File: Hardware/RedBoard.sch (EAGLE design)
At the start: 65 parts, among them IC3 LM1117, J2 ICSP, J3 POWER_JACKSUPER_BOMB_DIGITY, Q1 1A/60V/500mΩ, Q2 2N7002PW, U1 FT231XS, U2 MIC5205, U4 ATMEGA328P_TQFP, Y1 16MHz

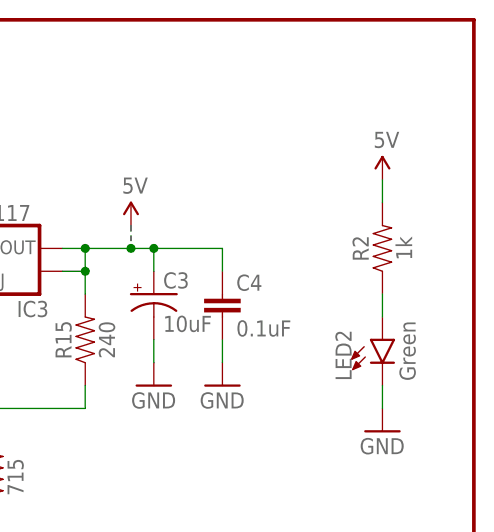
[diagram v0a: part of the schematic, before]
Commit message: Fixing LED silk, changing power LED resistor.
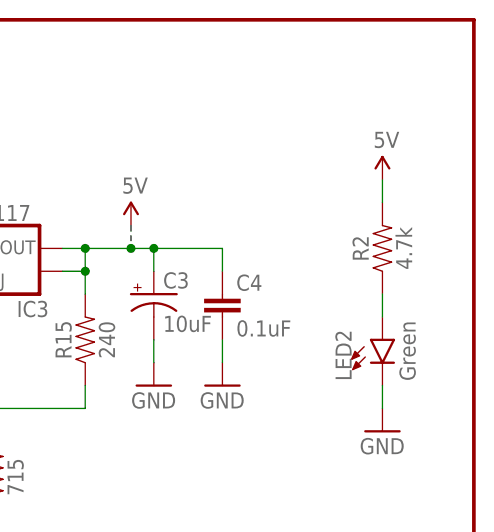
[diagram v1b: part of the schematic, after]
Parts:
- R2: value 1k -> 4.7k; device SparkFun-Resistors:1KOHM-0603-1/10W-1% -> SparkFun-Resistors:4.7KOHM-0603-1/10W-1%
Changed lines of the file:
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@@
 <part name="R1" library="SparkFun-Resistors" deviceset="1KOHM" device="-0603-1/10W-1%" value="1k"/>
 <part name="GND3" library="SparkFun" deviceset="GND" device=""/>
-<part name="R2" library="SparkFun-Resistors" deviceset="1KOHM" device="-0603-1/10W-1%" value="1k"/>
+<part name="R2" library="SparkFun-Resistors" deviceset="4.7KOHM" device="-0603-1/10W-1%" value="4.7k"/>
 <part name="U$2" library="SparkFun" deviceset="5V" device=""/>
 <part name="GND4" library="SparkFun" deviceset="GND" device=""/>

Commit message: Fixing PROD_ID on J2 and C10.
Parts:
- C10: device SparkFun-Capacitors:0.1UF-0603-25V-5% -> SparkFun-Capacitors:0.1UF-0603-25V-(+80/-20%)
- J2: PROD_ID (none) -> CONN-11415
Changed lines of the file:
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@@
 <?xml version="1.0" encoding="utf-8"?>
 <!DOCTYPE eagle SYSTEM "eagle.dtd">
-<eagle version="7.5.0">
+<eagle version="7.6.0">
 <drawing>
 <settings>
@@
 <part name="U$8" library="SparkFun" deviceset="5V" device=""/>
 <part name="C8" library="SparkFun-Capacitors" deviceset="0.1UF" device="-0603-25V-(+80/-20%)" value="0.1uF"/>
-<part name="C10" library="SparkFun-Capacitors" deviceset="0.1UF" device="-0603-25V-5%" value="0.1uF"/>
+<part name="C10" library="SparkFun-Capacitors" deviceset="0.1UF" device="-0603-25V-(+80/-20%)" value="0.1uF"/>
 <part name="GND24" library="SparkFun" deviceset="GND" device=""/>
 <part name="IC3" library="Testing" deviceset="V_REG_LM1117" device="ALT1" value="LM1117">
@@
 <part name="JP1" library="SparkFun-Aesthetics" deviceset="SFE_LOGO_NAME" device=".1_INCH"/>
 <part name="JP7" library="SparkFun-Aesthetics" deviceset="SFE_LOGO_FLAME" device=".1_INCH"/>
-<part name="J2" library="SparkFun-Connectors" deviceset="AVR_SPI_PROG_3X2" device="SMD" value="ICSP"/>
+<part name="J2" library="SparkFun-Connectors" deviceset="AVR_SPI_PROG_3X2" device="SMD" value="ICSP">
+<attribute name="PROD_ID" value="CONN-11415"/>
+</part>
 <part name="C6" library="SparkFun-Capacitors" deviceset="10UF-POLAR" device="-EIA3216-16V-10%(TANT)" value="10uF"/>
 <part name="GND14" library="SparkFun" deviceset="GND" device=""/>

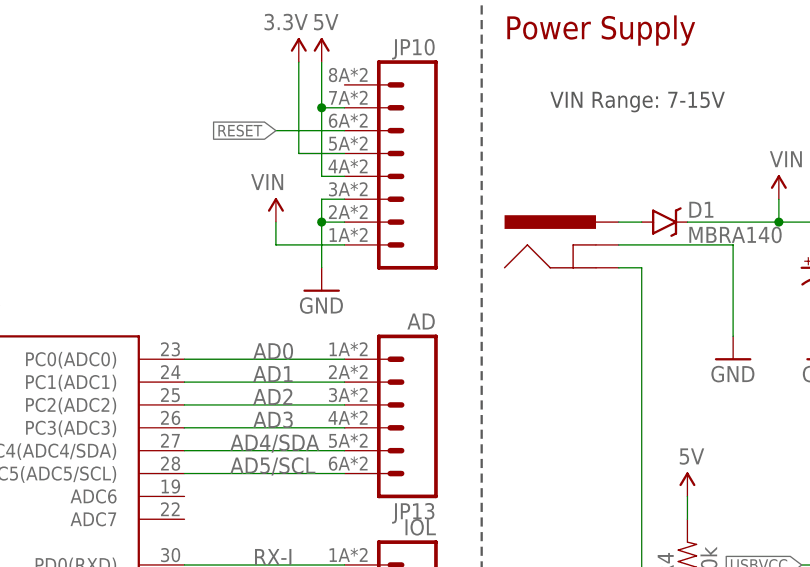
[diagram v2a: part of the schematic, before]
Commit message: Component Values Updated for 3D Model
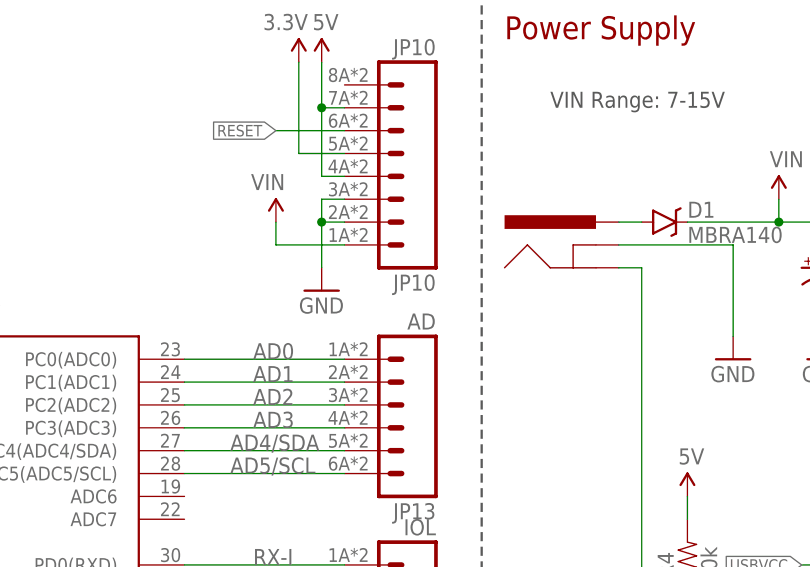
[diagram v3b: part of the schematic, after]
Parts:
- JP10: value (none) -> JP10
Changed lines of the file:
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@@
 <?xml version="1.0" encoding="utf-8"?>
 <!DOCTYPE eagle SYSTEM "eagle.dtd">
-<eagle version="7.6.0">
+<eagle version="7.7.0">
 <drawing>
 <settings>
@@
 <attribute name="PROD_ID" value="CONN-11219"/>
 </part>
-<part name="JP10" library="SparkFun-Connectors" deviceset="M08" device="SMD-COMBO">
+<part name="JP10" library="SparkFun-Connectors" deviceset="M08" device="SMD-COMBO" value="JP10">
 <attribute name="PROD_ID" value="CONN-10204"/>
 </part>

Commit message: Starting from BlackBoard x02
Starting from BlackBoard x02
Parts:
- removed C13, C9: 47pF, SparkFun-Capacitors:47PF-0603-50V-5%
- removed C14: 0.1uF, SparkFun-Capacitors:0.1UF-0603-25V-(+80/-20%)
- removed JP12: USB-MINIB-5PIN, SparkFun-Connectors:USB-MINIB-5PIN
- removed LED3: Red, SparkFun-LED:LED1206
- removed LED4: Yellow, SparkFun-LED:LED1206
- removed R10: 27, SparkFun-Resistors:27OHM-0603-1/10W-1%
- removed R7, R8, R9: 1k, SparkFun-Resistors:1KOHM-0603-1/10W-1%
- removed U1: FT231XS, SparkFun-IC-Comms:FT231XS
- added C11: 22pF, SparkFun-Capacitors:22PF-0603-50V-5%
- added C16: 1.0uF, SparkFun-Capacitors:1.0UF-16V-10%(0603)
- added C17: 10nF, SparkFun-Capacitors:10NF/10000PF-50V-10%(0603)
- added C18: 0.1uF, SparkFun-Capacitors:0.1UF-25V(+80/-20%)(0603)
- added D3: Yellow, SparkFun-LED:LED-YELLOW_HIDDENSILK
- added I/O: JUMPER-SMT_3_1-NC_TRACE_SILK, SparkFun-Jumpers:JUMPER-SMT_3_1-NC_TRACE_SILK
- added J1: AMP FCI 10103594-0001LF, SparkFun-Connectors:USB_MICRO-B_HALF_PTH_MILL
- added J4: (no value), SparkFun-Connectors:QWIIC_CONNECTORJS-1MM
- added LED5: GREEN, SparkFun-LED:LED-GREEN_HIDDENSILK
- added Q3: 2N7002PW, SparkFun-DiscreteSemi:MOSFET-NCH-2N7002PW
- added R12, R16: 4.7k, SparkFun-Resistors:4.7KOHM-0603-1/10W-1%
- added U3: AP2112-3.3V, SparkFun-PowerIC:V_REG_AP2112K-3.3V
- added Y2: 12MHz, USB Basic:CRYSTAL-GROUNDED3.2X2.5
- C7: value 1.0uF -> 22pF; device SparkFun-Capacitors:1.0UF-0603-16V-10% -> SparkFun-Capacitors:22PF-0603-50V-5%
- D1: value MBRA140 -> SS14TR
- F1: value 6V/0.5A -> PPTC_6V500MA; device SparkFun-Fuses:PTC-HALF_AMP -> SparkFun-Fuses:PPTC_6V500MA
- J2: value ICSP -> ISP
- JP10: value JP10 -> (none)
- JP11: value IOL -> JP11
- JP13: value AD -> (none)
- LED1: device SparkFun-LED:LED1206 -> SparkFun-LED:LED-BLUE_HIDDENSILK
- LED2: value Green -> GREEN; device SparkFun-LED:LED1206 -> SparkFun-LED:LED-GREEN_HIDDENSILK
- R1: value 1k -> 4.7k; device SparkFun-Resistors:1KOHM-0603-1/10W-1% -> SparkFun-Resistors:4.7KOHM-0603-1/10W-1%
- R11, R13: value 10k -> 2.2k; device SparkFun-Resistors:10KOHM-0603-1/10W-1% -> SparkFun-Resistors:2.2KOHM-0603-1/10W-1%
- R2: value 4.7k -> 10k; device SparkFun-Resistors:4.7KOHM-0603-1/10W-1% -> SparkFun-Resistors:10KOHM-0603-1/10W-1%
- R5: value 27 -> 2.2k; device SparkFun-Resistors:27OHM-0603-1/10W-1% -> SparkFun-Resistors:2.2KOHM-0603-1/10W-1%
- R6: value 1k -> 2.2k; device SparkFun-Resistors:1KOHM-0603-1/10W-1% -> SparkFun-Resistors:2.2KOHM-0603-1/10W-1%
- U2: value MIC5205 -> CH340G; device SparkFun-PowerIC:MIC52053.3V -> SparkFun-DigitalIC:CH340GSMD
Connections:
- removed net 3.3V_F: C14.1, Q2.G, R11.2, U1.!RESET, U1.3V3OUT, U1.VCCIO
- removed net D+: C9.1, JP12.D+, R10.1
- removed net D-: C13.1, JP12.D-, R5.1
- removed net DTR: C8.1, Q2.D, R13.1
- removed net FTDI_DTR: Q2.S, R11.1, U1.!DTR
- removed net N$10: LED4.A, R7.2
- removed net N$6: R5.2, U1.USBDM
- removed net N$7: R10.2, U1.USBDP
- removed net N$8: LED3.A, R6.2
- removed net RXD: R9.2, U1.RXD
- removed net RXLED: LED4.C, U1.CBUS1
- removed net TXD: R8.2, U1.TXD
- removed net TXLED: LED3.C, U1.CBUS2
- new net !DTR: C8.1, U2.!DTR
- new net LV_SCL: J4.4, Q2.S, R11.1
- new net LV_SDA: J4.3, Q3.S, R5.1
- new net N$11: C11.2, U2.XO, Y2.2
- new net N$12: C7.2, U2.XI, Y2.1
- new net N$13: J1.D-, U2.UD-
- new net N$14: J1.D+, U2.UD+
- new net N$5: LED5.A, R16.1
- new net N$9: D3.A, R12.1
- new net SHLD: J1.SHIELD
- new net V3: C17.1, U2.V3
- new net VCC: C18.1, C2.2, I/O.2, J2.2, R12.2, R13.2, R16.2, R2.2, R3.2, R6.2, TP1.1, U2.VCC, U4.AVCC, U4.VCC@4, U4.VCC@6
- net 3.3V: now also C16.1, I/O.1, J4.2, Q2.G, Q3.G, R11.2, R5.2, U3.OUT; no longer C7.1, U2.OUT
- net 5V: now also I/O.3, U3.EN, U3.IN; no longer C2.2, J2.2, R13.2, R2.2, R3.2, R6.1, R7.1, TP1.1, U2.EN, U2.IN, U4.AVCC, U4.VCC@4, U4.VCC@6
- net AD4/SDA: now also Q3.D, R6.1
- net AD5/SCL: now also Q2.D, R13.1
- net GND: now also C11.1, C16.2, C17.2, C18.2, C7.1, J1.GND, J4.1, U3.GND, Y2.GND; no longer C13.2, C14.2, C7.2, C9.2, JP12.GND, JP12.MTN1, JP12.MTN2, JP12.MTN3, JP12.MTN4, U1.GND@16, U1.GND@6
- net RX-I: now also D3.C, U2.TXD; no longer R8.1
- net TX-O: now also LED5.C, U2.RXD; no longer R9.1
- net USBVCC: no longer U1.VCC
- net VUSB: now also J1.VBUS; no longer JP12.VBUS
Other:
- note added: "3.3V 600mA Out"
- note added: "Board I/O Voltage"
- note added: "Jim Lindblom, N. Seidle"
- note added: "Qwiic"
- note added: "Qwiic 3.3V Conversion"
- note added: "To convert the board to 3.3V you must cut the jumper to 5V and use solder to close the jumper towards 3.3V."
- note added: "USB-to-Serial Converter"
- note added: "X01"
- note removed: "3.3V 150mA Out"
- note removed: "FT231XS (USB-to-Serial Converter)"
- note removed: "Jim Lindblom"
- note removed: "v22"
- moved on the sheet: C10, C12, C15, C2, C3, C4, C5, C6, C7, C8, D1, IC3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

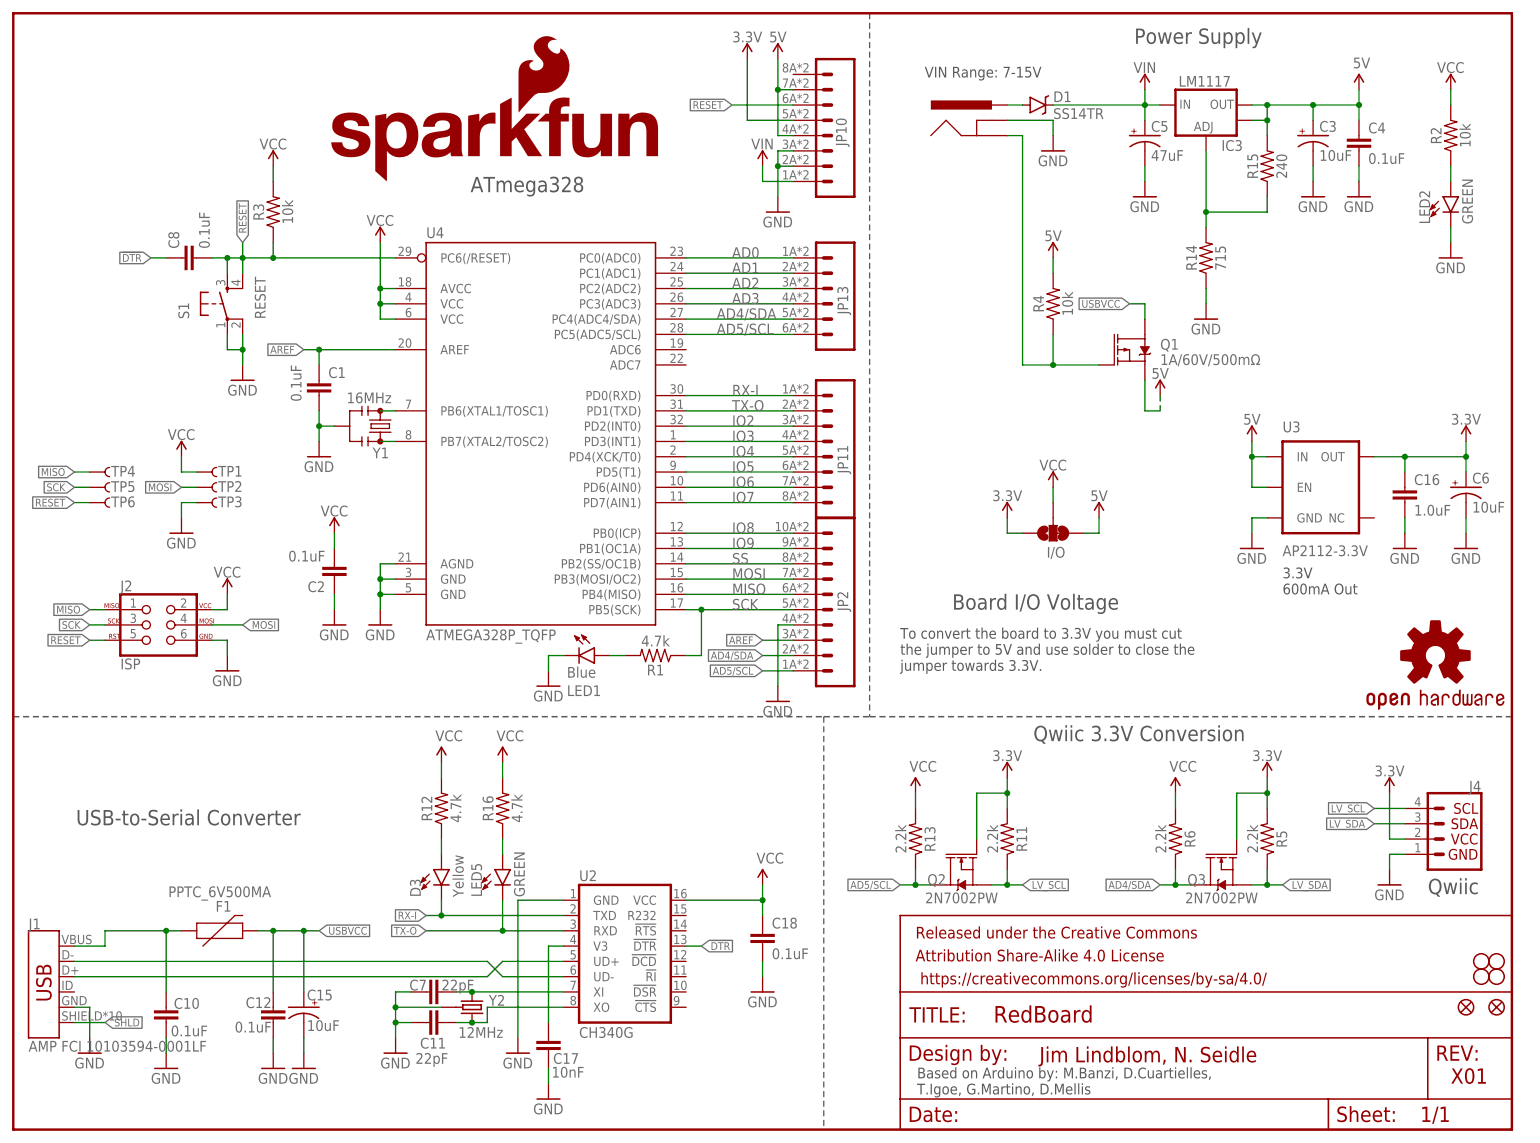
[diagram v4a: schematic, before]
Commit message: Silk Changes and USB changes
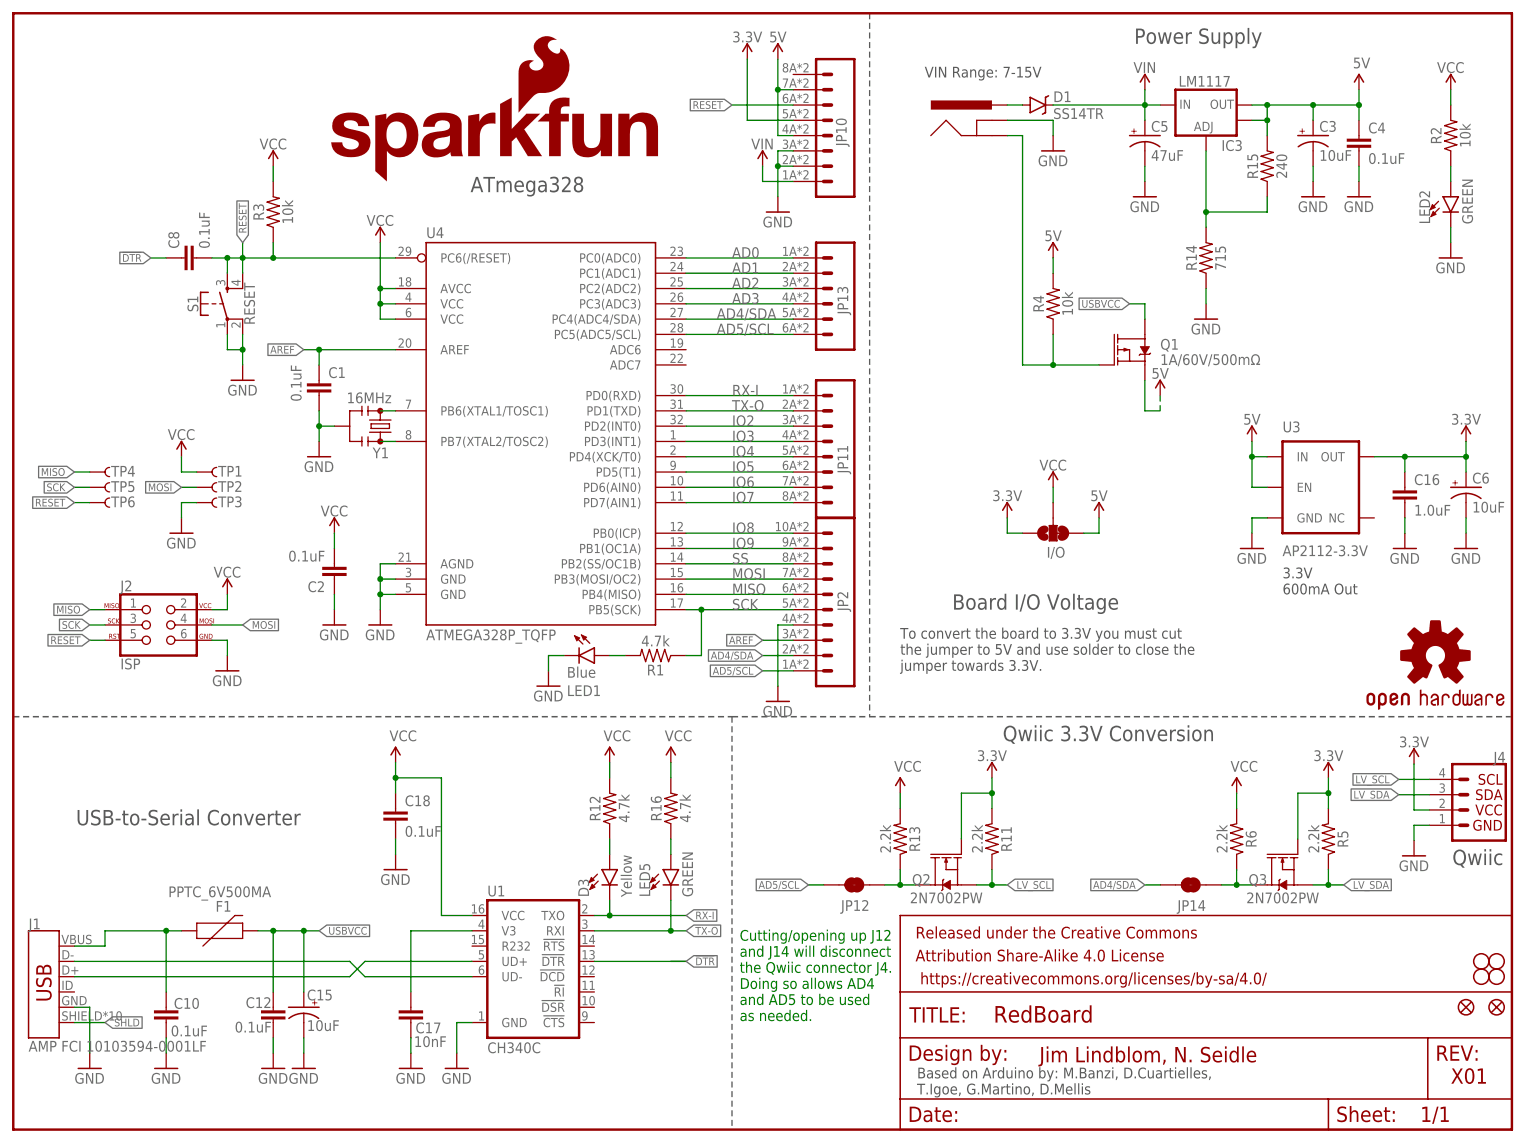
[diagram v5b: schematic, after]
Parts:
- removed C11, C7: 22pF, SparkFun-Capacitors:22PF-0603-50V-5%
- removed U2: CH340G, SparkFun-DigitalIC:CH340GSMD
- removed Y2: 12MHz, USB Basic:CRYSTAL-GROUNDED3.2X2.5
- added JP12, JP14: JUMPER-SMT_2_NC_TRACE_SILK, SparkFun-Jumpers:JUMPER-SMT_2_NC_TRACE_SILK
- added U1: CH340C, SparkFun-IC-Comms:CH340C
- S1: device SparkFun-Electromechanical:SWITCH_SPST_4_PINSQUARE -> SparkFun-Switches:MOMENTARY-SWITCH-SPST-2-SMD-5.2MM-TALL
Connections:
- removed net N$11: C11.2, U2.XO, Y2.2
- removed net N$12: C7.2, U2.XI, Y2.1
- removed net V3: C17.1, U2.V3
- new net N$6: C17.1, U1.V3
- new net N$7: JP12.1, Q2.D, R13.1
- new net N$8: JP14.1, Q3.D, R6.1
- net !DTR: now also U1.!DTR; no longer U2.!DTR
- net AD4/SDA: now also JP14.2; no longer Q3.D, R6.1
- net AD5/SCL: now also JP12.2; no longer Q2.D, R13.1
- net GND: now also U1.GND; no longer C11.1, C7.1, U2.GND, Y2.GND
- net N$13: now also U1.UD-; no longer U2.UD-
- net N$14: now also U1.UD+; no longer U2.UD+
- net RX-I: now also U1.TXO; no longer U2.TXD
- net TX-O: now also U1.RXI; no longer U2.RXD
- net VCC: now also U1.VCC; no longer U2.VCC
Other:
- note added: "Cutting/opening up J12 and J14 will disconnect the Qwiic connector J4. Doing so allows AD4 and AD5 to be used as needed."
- moved on the sheet: C17, C18, D3, J4, LED5, Q2, Q3, R11, R12, R13, R16, R5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
